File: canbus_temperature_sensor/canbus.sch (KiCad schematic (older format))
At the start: 1 part

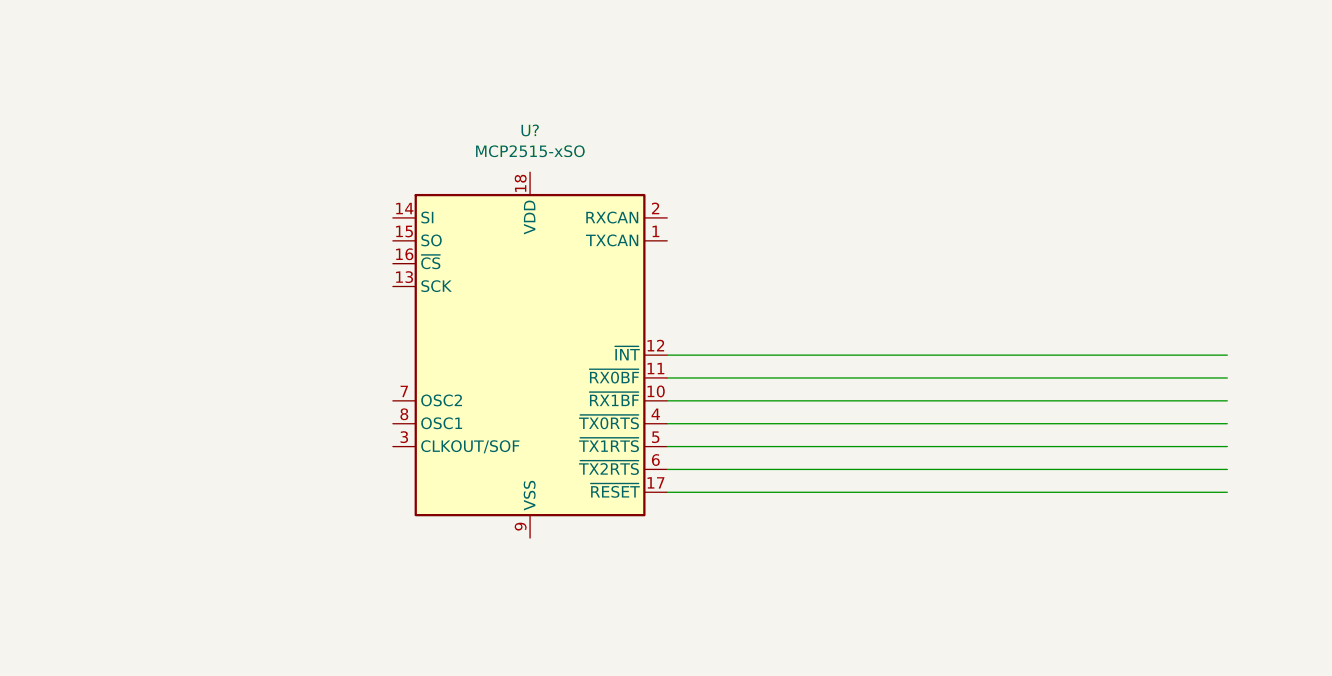
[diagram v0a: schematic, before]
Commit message: Further additions to canbus driver
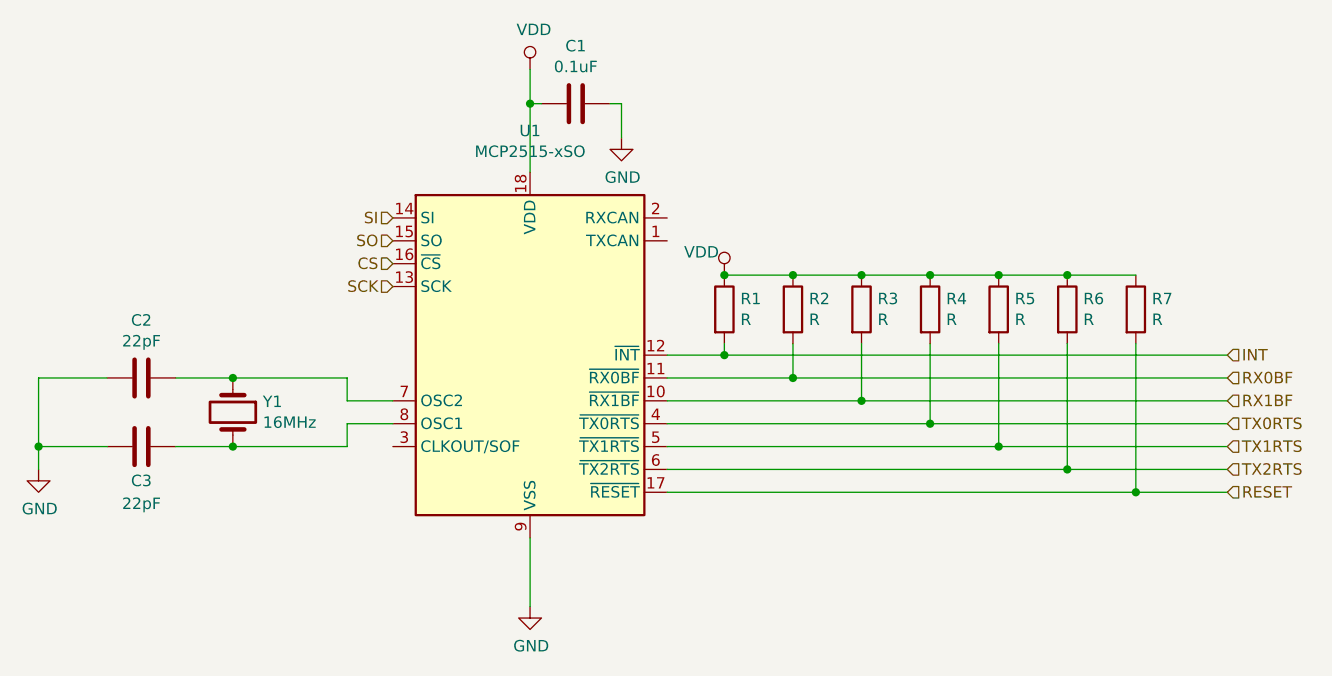
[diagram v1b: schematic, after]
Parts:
- added C1: 0.1uF, symbol Device:C
- added C2, C3: 22pF, symbol Device:C
- added R1, R2, R3, R4, R5, R6, R7: R, symbol Device:R
- added Y1: 16MHz, symbol Device:Crystal
- gave numbers to parts that had none: 1
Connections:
- net labels added: CS, GND, INT, RESET, RX0BF, RX1BF, SCK, SI, SO, TX0RTS, TX1RTS, TX2RTS, VDD
- wire segments 7 -> 45
